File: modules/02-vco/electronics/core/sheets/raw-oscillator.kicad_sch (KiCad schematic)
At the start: 56 parts, among them Q1 BC847BS, Q2 MMBT3906, Q3 J111, Q4 MMBFJ111, Q5 MMBT5551, U1 TL072, U2 TL072, U3 LM311

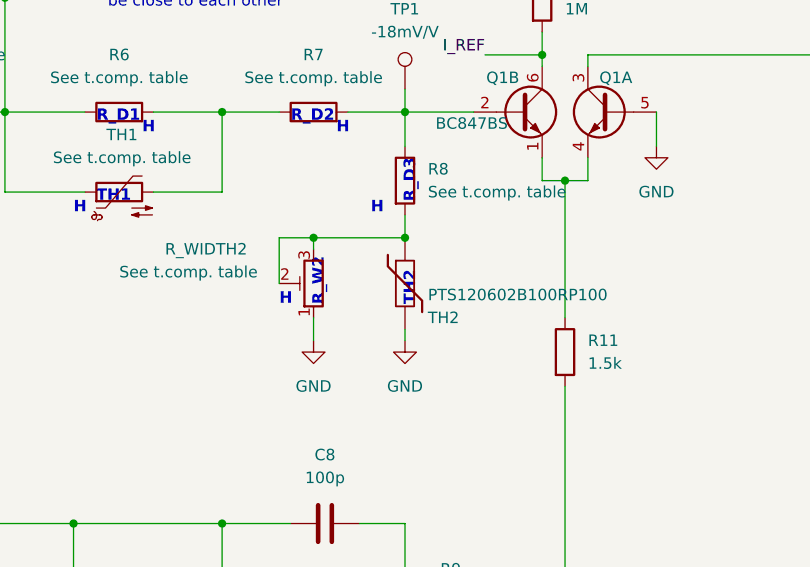
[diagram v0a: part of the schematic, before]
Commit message: Fix: Replace generic MMBT3906 with ON Semi for Q2
Q2 is the actuator in the master current servo loop (U1B → Q2) that sets the tail current for the exponential converter. The previous BOM specified the generic LCSC part C7420354, which JLCPCB silently substituted between production batches: batch 1 (Jan 2026) received a working part, while batches 2 and 3 received Zhuhai Hongjiacheng (R+O) MMBT3906 parts under the same C-code.

The R+O datasheet only characterizes hFE at IC = −10 mA and above, with no minimum specified at low collector currents. The circuit operates Q2 at sub-milliamp currents, where the substituted part has insufficient gain to close the servo loop. U1B saturates against the negative supply rail trying to compensate, leaving Q2's collector current stuck at a fixed (too-low) value regardless of CV input.
Symptoms across all affected boards (20+ units, fully uniform):

- VCO pitch ceiling at ~70 Hz
- Pitch plateaus and flattens above a certain CV — no further response to increasing CV
- R_BIAS1 trim has no effect on output (loop railed)
- TP1 floats at ~1V instead of being servoed to 0V
- U1B output pinned at −10.3V (TL072 negative rail)

Verified by swapping Q2 with a verified-genuine 2N3906 on two broken boards — both immediately tracked V/oct correctly across full CV range.
The replacement part ON Semi MMBT3906LT1G (LCSC C53444) explicitly specifies hFE ≥ 60 at IC = −0.1 mA in its datasheet, guaranteeing correct behavior in this circuit's operating range.
Changes:

BOM: Q2 LCSC part number changed from C7420354 → C53444
Schematic annotation updated to specify ON Semi MMBT3906LT1G
Production note added: "Q2 (C53444): Do not substitute. Must be ON Semi MMBT3906LT1G."
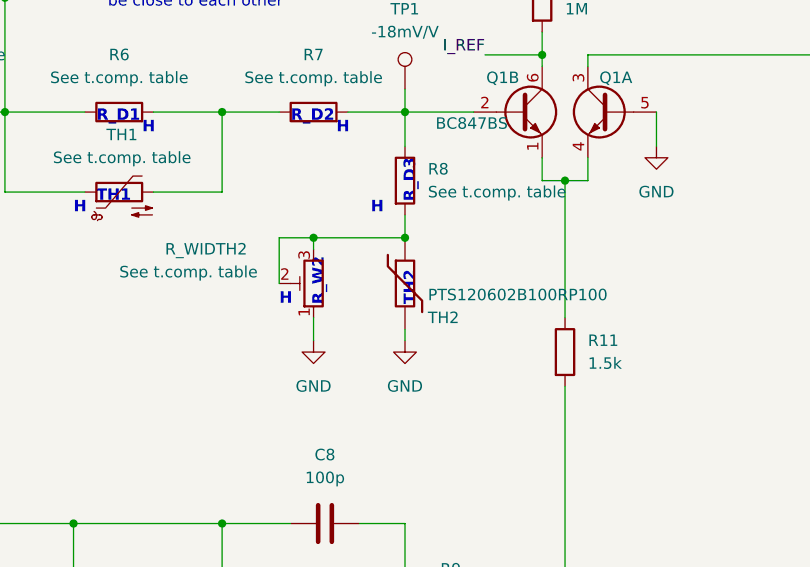
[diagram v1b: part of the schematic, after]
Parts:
- Q2: LCSC C7420354 -> C53444
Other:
- company: (none) -> Shmøergh
- title: (none) -> Moduleur VCO core

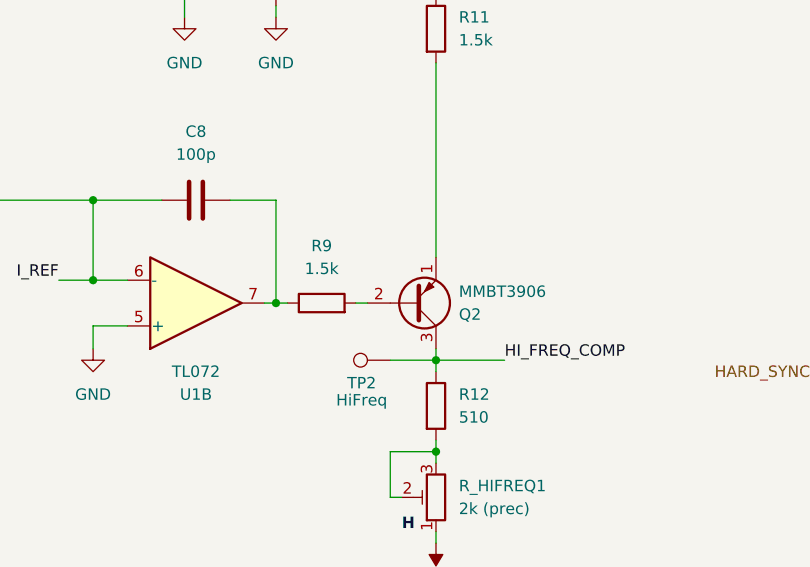
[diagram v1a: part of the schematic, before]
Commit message: Fixed Q2 footprint pin numbering
Previous production used the SMD MMBT3906 with traces routed to the wrong pads, leaving the transistor operating in reverse-active mode. This barely worked with some manufacturer's parts and failed entirely with others (specifically Zhuhai Hongjiacheng R+O parts in batches 2 and 3), producing a uniform pitch ceiling at ~70 Hz across all affected units.

For further information and manual fix, refer to VCO FIXLOG in the modules folder.
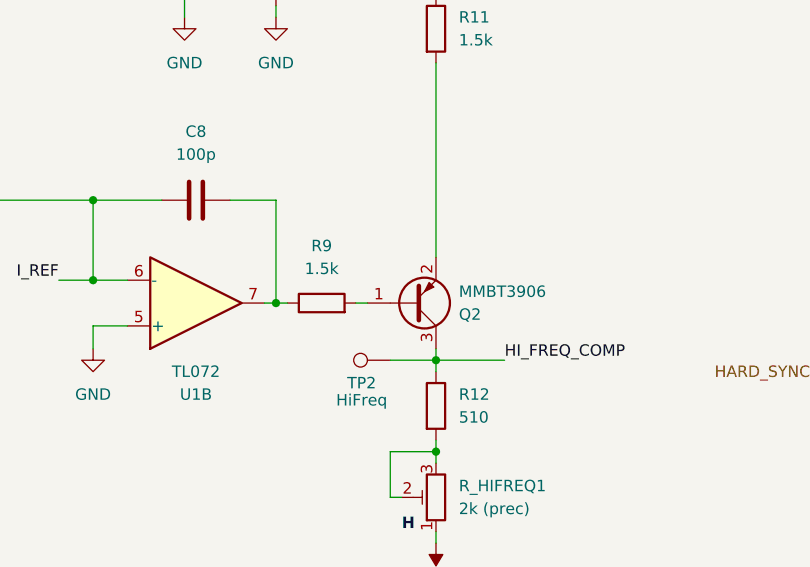
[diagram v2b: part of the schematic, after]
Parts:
- Q2: footprint Package_TO_SOT_SMD:SOT-23_Handsoldering -> Package_TO_SOT_SMD:SOT-23; symbol Transistor_BJT:2N3906 -> Transistor_BJT:MMBT3906
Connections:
- net at Q2.1 (B): now also R9.2; no longer R11.2
- net at Q2.2 (E): now also R11.2; no longer R9.2
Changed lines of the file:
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@@
 		(title "Moduleur VCO core")
 		(date "2026-05-24")
-		(rev "3")
+		(rev "4")
 		(company "Shmøergh")
 	)
@@
 	)
 	(symbol
-		(lib_id "Transistor_BJT:2N3906")
+		(lib_id "Transistor_BJT:MMBT3906")
 		(at 170.18 132.08 0)
 		(mirror x)
@@
 			)
 		)
-		(property "Footprint" "Package_TO_SOT_SMD:SOT-23_Handsoldering"
+		(property "Footprint" "Package_TO_SOT_SMD:SOT-23"
 			(at 175.26 130.175 0)
 			(hide yes)
@@
 			)
 		)
-		(property "Datasheet" "https://www.onsemi.com/pub/Collateral/2N3906-D.PDF"
+		(property "Datasheet" "https://www.onsemi.com/pdf/datasheet/pzt3906-d.pdf"
 			(at 170.18 132.08 0)
 			(hide yes)
@@
 			)
 		)
-		(property "Description" "-0.2A Ic, -40V Vce, Small Signal PNP Transistor, TO-92"
+		(property "Description" "-0.2A Ic, -40V Vce, Small Signal PNP Transistor, SOT-23"
 			(at 170.18 132.08 0)
 			(hide yes)
@@
 			(at 170.18 132.08 0)
 			(hide yes)
+			(show_name no)
+			(do_not_autoplace no)
+			(effects
+				(font
+					(size 1.27 1.27)
+				)
+			)
+		)
+		(property "Sim.Device" "PNP"
+			(at 170.18 132.08 0)
+			(hide yes)
+			(show_name no)
+			(do_not_autoplace no)
+			(effects
+				(font
+					(size 1.27 1.27)
+				)
+			)
+		)
+		(property "Sim.Pins" "1=B 2=E 3=C"
+			(at 170.18 132.08 0)
+			(hide yes)
